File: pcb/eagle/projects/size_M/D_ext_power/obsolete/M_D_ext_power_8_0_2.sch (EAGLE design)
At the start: 32 parts, among them U1 LM66100DCKR

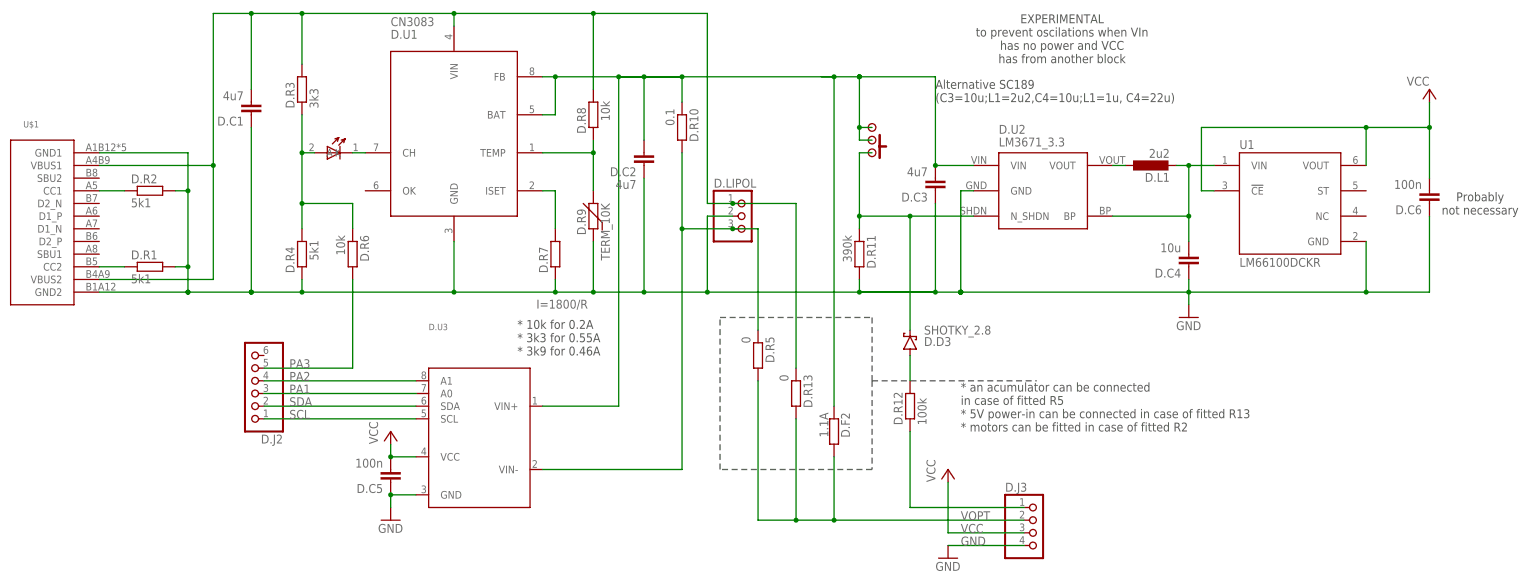
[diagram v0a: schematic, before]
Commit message: version 8 main changes * ideal diode separated 3v3 DC-DC to protect it from back current * smaller package of ina 219 * usage of tssop attiny v2 in adapter * and change of PA5 to PB2 with ^ and ~ (originally used for shield power switch - now PB3) * step motor shield * out signal for BT module
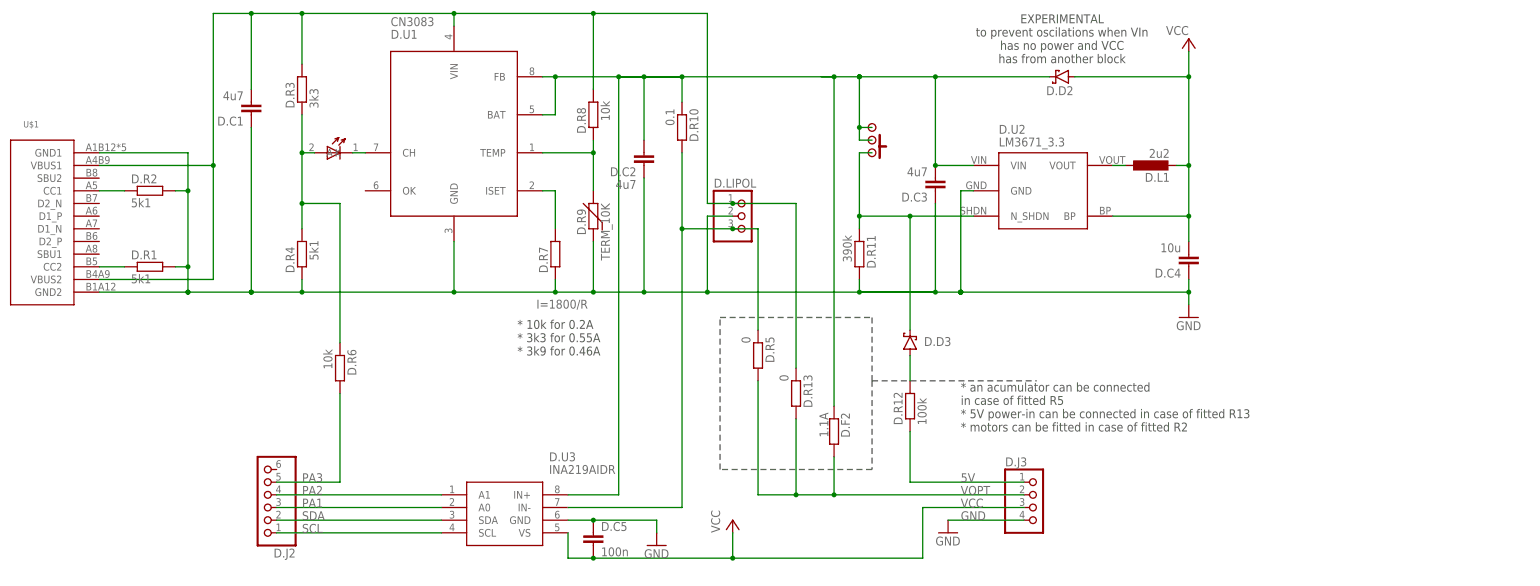
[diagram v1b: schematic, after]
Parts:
- removed D.C6: 100n, rcl:C-EUC0603
- removed U1: LM66100DCKR, LM66100DCKR:LM66100DCKR
- added D.D2: SHOTKY_2.8, hugo:SHOTKY_2.8
- D.C4: device rcl:C-EUC0603 -> rcl:C-EUC0805
- D.U3: value (none) -> INA219AIDR; device hugo:INA219 -> SamacSys_Parts:INA219AIDR
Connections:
- removed net VCC1: D.C4.2, D.L1.2, D.U2.BP, U1.VIN
- net GND: no longer D.C6.1, U1.GND
- net IN+: now also D.LIPOL.3, D.R10.2, D.R5.1, D.U3.IN-; no longer D.C2.2, D.C3.2, D.F2.1, D.ON/OFF/RESET.P$2, D.ON/OFF/RESET.P$3, D.R10.1, D.U1.BAT, D.U1.FB, D.U2.VIN, D.U3.VIN+
- net IN-: now also D.C2.2, D.C3.2, D.D2.C, D.F2.1, D.ON/OFF/RESET.P$2, D.ON/OFF/RESET.P$3, D.R10.1, D.U1.BAT, D.U1.FB, D.U2.VIN, D.U3.IN+; no longer D.LIPOL.3, D.R10.2, D.R5.1, D.U3.VIN-
- net VCC: now also D.C4.2, D.D2.A, D.L1.2, D.U2.BP, D.U3.VS; no longer D.C6.2, D.U3.VCC, U1.!CE, U1.VOUT
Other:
- note removed: "Alternative SC189 (C3=10u;L1=2u2,C4=10u;L1=1u, C4=22u)"
- note removed: "Probably not necessary"
- moved on the sheet: D.C5, D.J2, D.J3, D.R6, D.U3
